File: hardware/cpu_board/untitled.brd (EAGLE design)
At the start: 126.3 x 94.6 mm, 70 parts, among them IC1 MAX232ECWE, IC2 MAX232ECWE, IC3 AM29F040J, IC4 74HCT138D, IC5 LM2596S, J2 POWER_JACKSLT, U1 AS6C4008-55SIN

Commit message: PCB update
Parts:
- moved C2 64.8 mm to (-11.3, 7.32)
- moved C3 59.9 mm to (16.7, -7.29)
- moved R15 59.9 mm to (15.3, -7.29)
- moved U$4 59.5 mm to (42.2, 36.9)
- moved C15 45.3 mm to (4.06, -8.51)
- moved U$3 45.3 mm to (7.09, -6.92)
- moved C1 42.5 mm to (27.0, -10.8)
- moved R4 31.5 mm to (41.2, -7.21)
- moved R6 30.2 mm to (40.2, -3.91)
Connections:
- net !BUSACK: now also U$4.78
- net !BUSREQ: now also U$4.79
- net !INT: now also U$4.4
- net !IRQ1: now also U$4.5
- net !IRQ2: now also U$4.6
- net !NMI: now also U$4.1
- net !RD: now also U$4.70
- net !RST: now also U$4.80
- net !WAIT: now also U$4.77
- net !WR: now also U$4.69
- net 5V: now also U$4.32
- net A0: now also U$4.8
- net A1: now also U$4.9
- net A10: now also U$4.20
- net A11: now also U$4.21
- net A12: now also U$4.24
- net A13: now also U$4.25
- net A14: now also U$4.26
- net A15: now also U$4.27
- net A16: now also U$4.28
- net A17: now also U$4.29
- net A18: now also U$4.31
- net A2: now also U$4.10
- net A3: now also U$4.11
- net A4: now also U$4.13
- net A5: now also U$4.15
- net A6: now also U$4.16
- net A7: now also U$4.17
- net A8: now also U$4.18
- net A9: now also U$4.19
- net CLK: now also U$4.71
- net CTS1: now also U$4.46
- net CTS2: now also U$4.57
- net D0: now also U$4.35
- net D1: now also U$4.36
- net D2: now also U$4.37
- net D3: now also U$4.38
- net D4: now also U$4.39
- net D5: now also U$4.40
- net D6: now also U$4.41
- net D7: now also U$4.44
- net GND: now also U$4.12, U$4.34, U$4.72, U$4.73
- net RTS1: now also U$4.45
- net RXD1: now also U$4.49
- net RXD2: now also U$4.54
- net ST: now also U$4.7
- net TXD1: now also U$4.48
- net TXD2: now also U$4.52
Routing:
- net 5V: track 497.4 -> 451.8 mm
- net !IORQ: track 171.8 -> 137.6 mm
- net !M1: track 167.2 -> 133.3 mm
- net D1: track 159.3 -> 126.5 mm, vias 4 -> 2
- net !WR: track 196.8 -> 165.5 mm
- net !RD: track 205.6 -> 175.4 mm
- net CLK: track 101.2 -> 72.1 mm
- net D2: track 153.2 -> 129.1 mm, vias 4 -> 2
- net RTS1: track 52.6 -> 29.0 mm
- net CTS1: track 51.3 -> 28.0 mm
- net D3: track 131.3 -> 110.0 mm, vias 3 -> 1
- net !ROM_CS: track 47.4 -> 26.9 mm, vias 2 -> 1
- net RTS2: track 32.8 -> 12.2 mm
- net D5: track 124.8 -> 104.5 mm, vias 3 -> 1
- net D0: track 146.4 -> 126.2 mm, vias 3 -> 2
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
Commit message: PCB updated
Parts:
- removed U$3: ASE, crystal:ASE
- added C16, C32: (no value), rcl:C0603
- added Y1: CRYSTAL-GROUNDEDSMD-5X3.2, SparkFun-Clocks:CRYSTAL-SMD-5X3.2-4PAD
- R4, R6: device rcl:R0603 -> rcl:R0402
- moved C1 56.9 mm to (57.1, 37.4), turned to 90 degrees
- moved R4 32.9 mm to (35.2, 25.2)
- moved R6 24.1 mm to (32.0, 18.7)
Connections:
- removed net OSC_IN: U$3.3
- new net EXTAL: C16.1, U$4.76, Y1.3
- new net XTAL: C32.1, U$4.74, Y1.1
- net 5V: no longer U$3.4
- net GND: now also C16.2, C32.2, Y1.2, Y1.4; no longer U$3.2
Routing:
- net !WR: track 165.5 -> 197.6 mm
- net !RD: track 175.4 -> 206.7 mm
- net CLK: track 72.1 -> 102.5 mm
- net D0: track 126.2 -> 142.7 mm
- net D1: track 126.5 -> 142.1 mm
- net D2: track 129.1 -> 144.4 mm
- net D3: track 110.0 -> 125.0 mm
- net XTAL: track 0.00 -> 8.82 mm
- net EXTAL: track 0.00 -> 6.46 mm
- net !INT: track 74.7 -> 78.8 mm
- net 5V: track 451.8 -> 455.6 mm, vias 11 -> 12
- net !IRQ2: track 108.4 -> 109.9 mm
- net !IRQ1: track 103.8 -> 104.9 mm

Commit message: PCB updated
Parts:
- removed C16, C32: (no value), rcl:C0603
- removed Y1: CRYSTAL-GROUNDEDSMD-5X3.2, SparkFun-Clocks:CRYSTAL-SMD-5X3.2-4PAD
- added R11: (no value), rcl:R0603
- added U$3: ASE, crystal:ASE
- R15: device rcl:R0402 -> rcl:R0603
- moved R15 54.1 mm to (30.2, 44.7), turned to 180 degrees
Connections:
- new net N$26: IC4.6, R11.1
- net !IORQ: now also U$4.65
- net !M1: no longer IC4.6
- net 5V: now also R11.2, U$3.4
- net EXTAL: now also U$3.3; no longer C16.1, Y1.3
- net GND: now also U$3.2; no longer C16.2, C32.2, Y1.2, Y1.4
- net N$25: now also U$4.59
- net XTAL: no longer C32.1, Y1.1
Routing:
- net !M1: track 133.3 -> 0.00 mm, vias 1 -> 0
- net !IORQ: track 137.6 -> 169.7 mm
- net TXD2: track 10.3 -> 38.6 mm
- net RTS1: track 29.0 -> 56.1 mm
- net RXD2: track 8.88 -> 35.5 mm
- net CTS1: track 28.0 -> 53.9 mm
- net TXD1: track 24.8 -> 49.1 mm
- net CTS2: track 13.2 -> 35.3 mm
- net RXD1: track 26.4 -> 44.7 mm
- net N$26: track 0.00 -> 12.2 mm, vias 0 -> 1
- net XTAL: track 8.82 -> 0.00 mm
- net N$25: track 0.00 -> 8.32 mm
- net RTS2: track 12.2 -> 4.62 mm
- net EXTAL: track 6.46 -> 3.40 mm
- net 5V: track 455.6 -> 458.6 mm, vias 12 -> 13
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
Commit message: Minor update
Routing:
- net RTS2: track 4.62 -> 10.8 mm
- net CTS2: track 35.3 -> 33.6 mm
- net TXD2: track 38.6 -> 40.0 mm
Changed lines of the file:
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@@
 <contactref element="C12" pad="2"/>
 <contactref element="C11" pad="2"/>
-<via x="17.145" y="42.545" extent="1-16" drill="0.6" diameter="1.4224" shape="octagon"/>
+<via x="17.145" y="45.72" extent="1-16" drill="0.6" diameter="1.4224" shape="octagon"/>
 <via x="24.0792" y="67.31" extent="1-16" drill="0.6" diameter="1.4224" shape="octagon"/>
 <via x="15.875" y="48.895" extent="1-16" drill="0.6" diameter="1.4224" shape="octagon"/>
@@
 <signal name="TXD2">
 <contactref element="IC1" pad="11"/>
-<wire x1="17.78" y1="30.9372" x2="17.78" y2="34.29" width="0.4064" layer="16"/>
-<via x="17.78" y="34.29" extent="1-16" drill="0.6" diameter="1.4224" shape="octagon"/>
+<wire x1="17.78" y1="30.9372" x2="17.78" y2="40.5892" width="0.4064" layer="16"/>
+<via x="17.78" y="40.5892" extent="1-16" drill="0.6" diameter="1.4224" shape="octagon"/>
 <contactref element="U$4" pad="52"/>
-<wire x1="17.78" y1="34.29" x2="17.78" y2="35.9664" width="0.3048" layer="1"/>
-<wire x1="17.78" y1="35.9664" x2="25.4" y2="43.5864" width="0.3048" layer="1"/>
-<wire x1="25.4" y1="43.5864" x2="25.4" y2="45.8216" width="0.3048" layer="1"/>
-<wire x1="25.4" y1="45.8216" x2="27.7368" y2="48.1584" width="0.3048" layer="1"/>
-<wire x1="27.7368" y1="48.1584" x2="41.6052" y2="48.1584" width="0.3048" layer="1"/>
+<wire x1="26.9494" y1="48.1584" x2="41.6052" y2="48.1584" width="0.3048" layer="1"/>
 <wire x1="41.6052" y1="48.1584" x2="43.0402" y2="46.7234" width="0.3048" layer="1"/>
 <wire x1="43.0402" y1="45.3254" x2="43.0402" y2="46.7234" width="0.3048" layer="1"/>
+<wire x1="17.78" y1="40.5892" x2="19.3802" y2="40.5892" width="0.3048" layer="1"/>
+<wire x1="26.9494" y1="48.1584" x2="19.3802" y2="40.5892" width="0.3048" layer="1"/>
 </signal>
 <signal name="RTS2">
 <contactref element="IC1" pad="10"/>
-<wire x1="16.51" y1="30.9372" x2="16.51" y2="35.56" width="0.4064" layer="16"/>
-<via x="16.51" y="35.56" extent="1-16" drill="0.6" diameter="1.4224" shape="octagon"/>
+<wire x1="16.51" y1="30.9372" x2="16.51" y2="41.783" width="0.4064" layer="16"/>
+<via x="16.51" y="41.783" extent="1-16" drill="0.6" diameter="1.4224" shape="octagon"/>
 </signal>
 <signal name="RXD2">
 <contactref element="IC1" pad="12"/>
-<wire x1="19.05" y1="30.9372" x2="19.05" y2="35.56" width="0.4064" layer="16"/>
-<via x="19.05" y="35.56" extent="1-16" drill="0.6" diameter="1.4224" shape="octagon"/>
+<wire x1="19.05" y1="30.9372" x2="19.05" y2="39.3954" width="0.4064" layer="16"/>
+<via x="19.05" y="39.3954" extent="1-16" drill="0.6" diameter="1.4224" shape="octagon"/>
 <contactref element="U$4" pad="54"/>
-<wire x1="19.05" y1="36.0172" x2="26.0096" y2="42.9768" width="0.3048" layer="1"/>
-<wire x1="26.0096" y1="42.9768" x2="26.0096" y2="45.5676" width="0.3048" layer="1"/>
-<wire x1="26.0096" y1="45.5676" x2="27.9908" y2="47.5488" width="0.3048" layer="1"/>
-<wire x1="27.9908" y1="47.5488" x2="40.6146" y2="47.5488" width="0.3048" layer="1"/>
+<wire x1="27.2034" y1="47.5488" x2="40.6146" y2="47.5488" width="0.3048" layer="1"/>
 <wire x1="40.6146" y1="47.5488" x2="41.4402" y2="46.7232" width="0.3048" layer="1"/>
 <wire x1="41.4402" y1="45.3254" x2="41.4402" y2="46.7232" width="0.3048" layer="1"/>
-<wire x1="19.05" y1="35.56" x2="19.05" y2="36.0172" width="0.3048" layer="1"/>
+<wire x1="27.2034" y1="47.5488" x2="19.05" y2="39.3954" width="0.3048" layer="1"/>
 </signal>
 <signal name="CTS2">
 <contactref element="IC1" pad="9"/>
-<wire x1="15.24" y1="30.9372" x2="15.24" y2="33.02" width="0.4064" layer="16"/>
-<via x="15.24" y="33.02" extent="1-16" drill="0.6" diameter="1.4224" shape="octagon"/>
+<wire x1="15.24" y1="30.9372" x2="15.24" y2="33.9344" width="0.4064" layer="16"/>
+<via x="15.24" y="33.9344" extent="1-16" drill="0.6" diameter="1.4224" shape="octagon"/>
 <contactref element="U$4" pad="57"/>
-<wire x1="15.24" y1="33.02" x2="18.161" y2="33.02" width="0.3048" layer="1"/>
-<wire x1="20.2184" y1="36.322" x2="26.6192" y2="42.7228" width="0.3048" layer="1"/>
-<wire x1="26.6192" y1="42.7228" x2="26.6192" y2="45.3136" width="0.3048" layer="1"/>
-<wire x1="26.6192" y1="45.3136" x2="28.2448" y2="46.9392" width="0.3048" layer="1"/>
 <wire x1="28.2448" y1="46.9392" x2="38.6842" y2="46.9392" width="0.3048" layer="1"/>
 <wire x1="38.6842" y1="46.9392" x2="39.0402" y2="46.5832" width="0.3048" layer="1"/>
 <wire x1="39.0402" y1="45.3254" x2="39.0402" y2="46.5832" width="0.3048" layer="1"/>
-<wire x1="18.161" y1="33.02" x2="20.2184" y2="35.0774" width="0.3048" layer="1"/>
-<wire x1="20.2184" y1="35.0774" x2="20.2184" y2="36.322" width="0.3048" layer="1"/>
+<wire x1="15.24" y1="33.9344" x2="28.2448" y2="46.9392" width="0.3048" layer="1"/>
 </signal>
 <signal name="N$20">

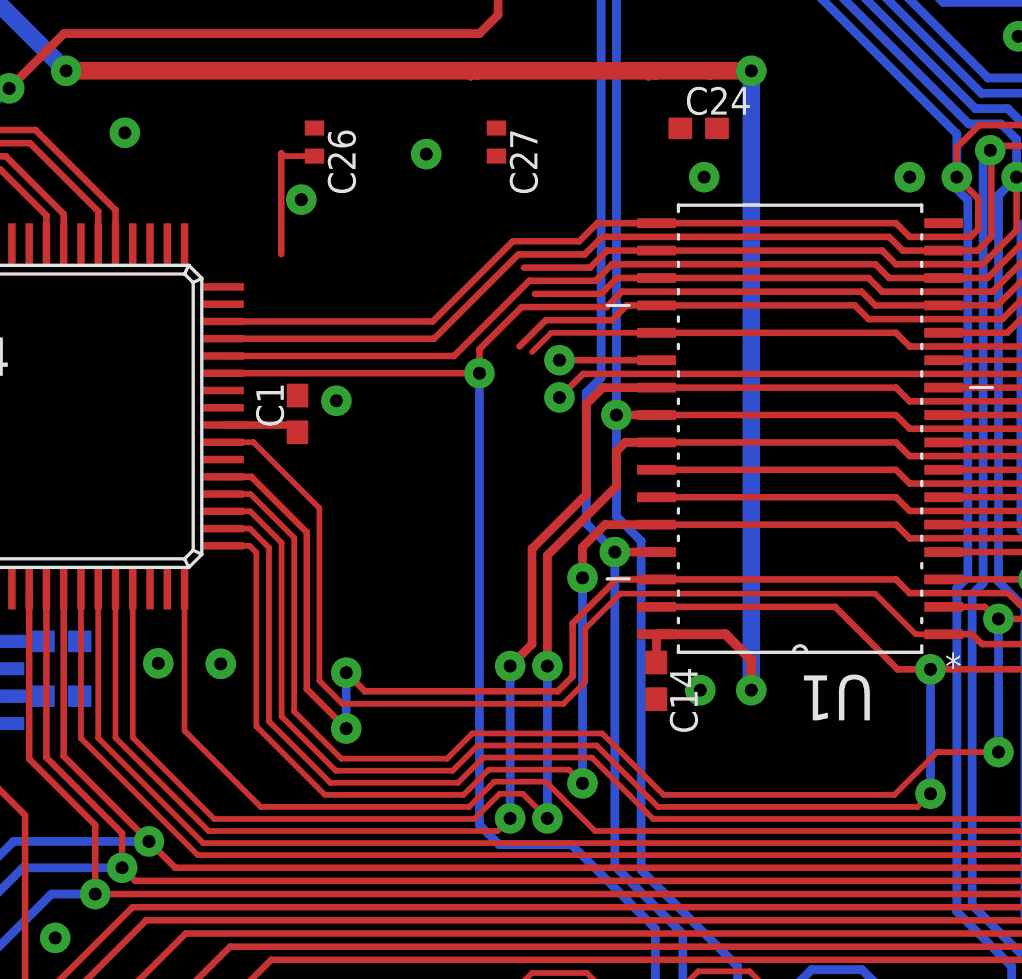
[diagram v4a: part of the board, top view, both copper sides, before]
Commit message: Data lines routed
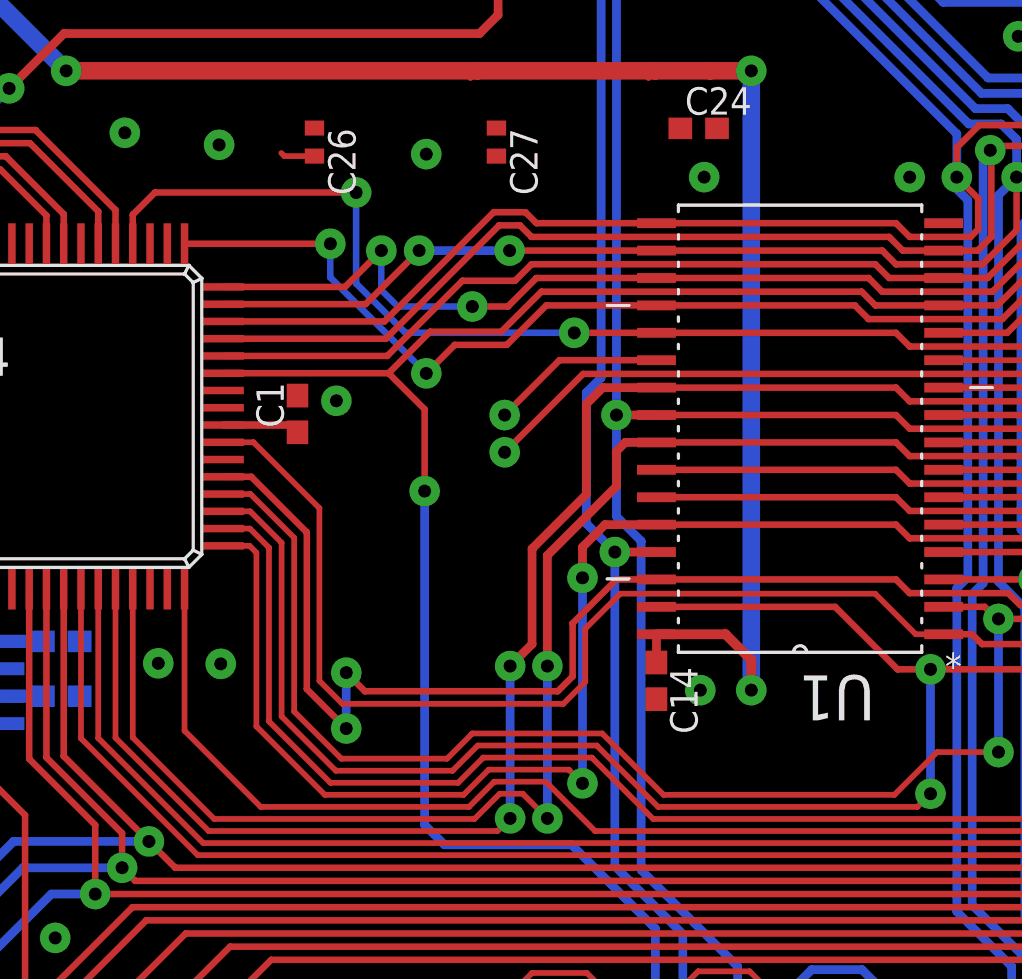
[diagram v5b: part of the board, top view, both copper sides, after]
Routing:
- net D7: track 77.6 -> 102.7 mm, vias 1 -> 3
- net D6: track 105.5 -> 125.2 mm, vias 1 -> 3
- net D5: track 104.5 -> 122.0 mm, vias 1 -> 3
- net D4: track 106.7 -> 121.3 mm, vias 1 -> 3
- net GND: track 71.1 -> 66.4 mm
- net !ROM_CS: track 26.9 -> 30.5 mm
- net !RAM_CS: track 4.50 -> 8.09 mm
- net D0: track 142.7 -> 145.3 mm

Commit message: Another update
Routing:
- net !RST: track 165.2 -> 168.0 mm, vias 4 -> 2
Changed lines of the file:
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@@
 <wire x1="83.8581" y1="42.4688" x2="83.2231" y2="43.1038" width="0.3048" layer="1"/>
 <wire x1="83.2231" y1="43.1038" x2="68.3768" y2="43.1038" width="0.3048" layer="1"/>
-<via x="62.9666" y="33.8644" extent="1-16" drill="0.6" diameter="1.4224" shape="octagon"/>
+<via x="62.9666" y="26.8794" extent="1-16" drill="0.6" diameter="1.4224" shape="octagon"/>
 <wire x1="98.1456" y1="46.609" x2="97.3328" y2="47.4218" width="0.3048" layer="1"/>
-<wire x1="62.9666" y1="33.8644" x2="62.9666" y2="18.3896" width="0.4064" layer="16"/>
+<wire x1="62.9666" y1="26.8794" x2="62.9666" y2="18.3896" width="0.4064" layer="16"/>
 <wire x1="62.9666" y1="18.3896" x2="63.881" y2="17.4752" width="0.4064" layer="16"/>
 <wire x1="63.881" y1="17.4752" x2="69.7738" y2="17.4752" width="0.4064" layer="16"/>
@@
 <wire x1="66.5226" y1="41.2496" x2="68.3768" y2="43.1038" width="0.3048" layer="1"/>
 <wire x1="63.2206" y1="41.2496" x2="61.2964" y2="39.3254" width="0.3048" layer="1"/>
-<wire x1="62.9666" y1="33.8644" x2="62.9666" y2="37.6552" width="0.3048" layer="1"/>
+<wire x1="62.9666" y1="26.8794" x2="62.9666" y2="37.6552" width="0.3048" layer="1"/>
 <wire x1="62.9666" y1="37.6552" x2="61.2964" y2="39.3254" width="0.3048" layer="1"/>
 </signal>
@@
 <wire x1="59.7916" y1="43.4848" x2="62.0776" y2="41.1988" width="0.3048" layer="16"/>
 <wire x1="50.4698" y1="47.7012" x2="59.7916" y2="47.7012" width="0.3048" layer="1"/>
-<via x="69.9008" y="41.1988" extent="1-16" drill="0.6" diameter="1.4224" shape="octagon"/>
-<wire x1="73.7108" y1="41.1988" x2="69.9008" y2="41.1988" width="0.3048" layer="1"/>
-<wire x1="69.9008" y1="41.1988" x2="62.0776" y2="41.1988" width="0.3048" layer="16"/>
+<via x="69.0372" y="41.2242" extent="1-16" drill="0.6" diameter="1.4224" shape="octagon"/>
+<wire x1="73.7108" y1="41.1988" x2="69.0372" y2="41.2242" width="0.3048" layer="1"/>
+<wire x1="69.0372" y1="41.2242" x2="62.0776" y2="41.1988" width="0.3048" layer="16"/>
 </signal>
 <signal name="!IORQ">
@@
 <wire x1="38.1162" y1="23.0886" x2="39.5732" y2="23.0886" width="0.4064" layer="16"/>
 <wire x1="39.5732" y1="23.0886" x2="39.9034" y2="23.4188" width="0.4064" layer="16"/>
-<wire x1="70.4342" y1="60.1218" x2="70.4342" y2="67.9958" width="0.4064" layer="16"/>
 <wire x1="70.4342" y1="67.9958" x2="73.7108" y2="71.2724" width="0.4064" layer="16"/>
 <wire x1="73.7108" y1="71.2724" x2="93.8276" y2="71.2724" width="0.4064" layer="16"/>
 <wire x1="93.8276" y1="71.2724" x2="94.9325" y2="70.1675" width="0.4064" layer="16"/>
 <wire x1="94.9325" y1="66.31" x2="94.9325" y2="70.1675" width="0.4064" layer="16"/>
-<wire x1="69.5706" y1="59.2582" x2="70.4342" y2="60.1218" width="0.4064" layer="16"/>
-<via x="43.7134" y="52.5272" extent="1-16" drill="0.6" diameter="1.4224" shape="octagon"/>
-<wire x1="65.5066" y1="55.0672" x2="66.3702" y2="55.9308" width="0.4064" layer="1"/>
-<wire x1="66.3702" y1="55.9308" x2="66.3702" y2="59.2582" width="0.4064" layer="1"/>
-<via x="66.3702" y="59.2582" extent="1-16" drill="0.6" diameter="1.4224" shape="octagon"/>
-<wire x1="66.3702" y1="59.2582" x2="69.5706" y2="59.2582" width="0.4064" layer="16"/>
-<wire x1="65.5066" y1="55.0672" x2="46.2534" y2="55.0672" width="0.4064" layer="1"/>
-<wire x1="46.2534" y1="55.0672" x2="43.7134" y2="52.5272" width="0.4064" layer="1"/>
-<wire x1="39.9034" y1="23.4188" x2="39.9034" y2="29.845" width="0.4064" layer="16"/>
-<wire x1="39.9034" y1="29.845" x2="39.9034" y2="48.7172" width="0.4064" layer="16"/>
-<wire x1="39.9034" y1="48.7172" x2="43.7134" y2="52.5272" width="0.4064" layer="16"/>
+<wire x1="39.9034" y1="23.4188" x2="39.9034" y2="29.972" width="0.4064" layer="16"/>
 <wire x1="38.1162" y1="23.0886" x2="36.83" y2="23.0886" width="0.6096" layer="16"/>
 <wire x1="36.83" y1="23.0886" x2="35.1913" y2="23.0886" width="0.6096" layer="16"/>
@@
 <wire x1="31.6402" y1="31.3254" x2="31.5976" y2="31.3254" width="0.3048" layer="1"/>
 <wire x1="31.5976" y1="31.3254" x2="31.5976" y2="29.972" width="0.3048" layer="1"/>
-<wire x1="31.5976" y1="29.972" x2="39.8018" y2="29.972" width="0.4064" layer="16"/>
-<wire x1="39.8018" y1="29.972" x2="39.9034" y2="29.845" width="0.4064" layer="16"/>
+<wire x1="31.5976" y1="29.972" x2="39.9034" y2="29.972" width="0.4064" layer="16"/>
+<wire x1="70.4342" y1="67.9958" x2="70.4342" y2="39.4208" width="0.4064" layer="16"/>
+<wire x1="70.4342" y1="39.4208" x2="69.7484" y2="38.735" width="0.4064" layer="16"/>
+<wire x1="69.7484" y1="38.735" x2="69.7484" y2="32.512" width="0.4064" layer="16"/>
+<wire x1="39.9034" y1="29.972" x2="67.2084" y2="29.972" width="0.4064" layer="16"/>
+<wire x1="67.2084" y1="29.972" x2="69.7484" y2="32.512" width="0.4064" layer="16"/>
 </signal>
 <signal name="!M1">

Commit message: PCB update
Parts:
- moved C24 75.9 mm to (32.3, -11.5), turned to 270 degrees
- moved C27 71.4 mm to (30.1, -11.6)
- moved C26 68.4 mm to (28.0, -11.6)
- moved C21 1.91 mm to (45.3, 64.1)
- moved C20 1.91 mm to (31.9, 79.4)
- moved C23 1.91 mm to (39.6, 64.8)
- moved C28 1.91 mm to (29.9, 69.4)
- moved D1 1.91 mm to (27.1, 72.4)
- moved IC5 1.91 mm to (33.0, 61.6)
- moved L2 1.91 mm to (52.8, 71.5)
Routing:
- net 5V: track 458.6 -> 479.8 mm, vias 13 -> 14
- net GND: track 66.4 -> 65.0 mm
- net N$22: track 27.4 -> 26.2 mm

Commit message: PCB update
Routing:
- net 5V: track 479.8 -> 476.4 mm
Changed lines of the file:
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@@
 <wire x1="59.69" y1="86.5452" x2="59.69" y2="86.5486" width="1.0668" layer="1"/>
 <contactref element="C22" pad="+"/>
-<wire x1="59.69" y1="86.5486" x2="59.69" y2="88.9" width="1.0668" layer="1"/>
-<wire x1="59.69" y1="88.9" x2="59.69" y2="89.6366" width="1.0668" layer="1"/>
+<wire x1="59.69" y1="86.5486" x2="59.69" y2="89.6366" width="1.0668" layer="1"/>
 <wire x1="27.7994" y1="56.9468" x2="27.7994" y2="50.165" width="0.8128" layer="16"/>
 <wire x1="27.7994" y1="50.165" x2="27.7994" y2="44.7412" width="0.8128" layer="16"/>
@@
 <wire x1="52.2732" y1="56.9468" x2="55.88" y2="53.34" width="0.8128" layer="16"/>
 <via x="91.1216" y="59.1194" extent="1-16" drill="0.6" diameter="1.4224" shape="octagon"/>
-<wire x1="109.22" y1="91.44" x2="119.0752" y2="81.5848" width="1.0668" layer="1"/>
+<wire x1="114.1114" y1="86.5486" x2="119.0752" y2="81.5848" width="1.0668" layer="1"/>
 <wire x1="119.0752" y1="56.388" x2="119.0752" y2="65.20024375" width="1.0668" layer="1"/>
 <wire x1="119.0752" y1="65.20024375" x2="119.0752" y2="81.5848" width="1.0668" layer="1"/>
@@
 <wire x1="102.66524375" y1="65.20024375" x2="100.0506" y2="62.5856" width="1.0668" layer="1"/>
 <wire x1="100.0506" y1="59.1194" x2="100.0506" y2="62.5856" width="1.0668" layer="1"/>
-<wire x1="59.69" y1="88.9" x2="68.58" y2="88.9" width="1.0668" layer="1"/>
-<wire x1="68.58" y1="88.9" x2="71.12" y2="91.44" width="1.0668" layer="1"/>
-<wire x1="71.12" y1="91.44" x2="102.235" y2="91.44" width="1.0668" layer="1"/>
-<wire x1="102.235" y1="91.44" x2="109.22" y2="91.44" width="1.0668" layer="1"/>
 <contactref element="C24" pad="1"/>
 <contactref element="C26" pad="1"/>
@@
 <contactref element="C15" pad="1"/>
 <wire x1="4.064" y1="-7.659" x2="4.064" y2="-6.0979" width="0.6096" layer="1"/>
-<wire x1="102.0064" y1="91.2114" x2="102.235" y2="91.44" width="0.6096" layer="1"/>
 <wire x1="76.1864" y1="53.3536" x2="76.2" y2="53.34" width="0.3048" layer="1"/>
 <contactref element="U$4" pad="32"/>
@@
 <wire x1="55.88" y1="53.34" x2="55.88" y2="39.3836" width="0.8128" layer="16"/>
 <wire x1="55.88" y1="39.3836" x2="58.674" y2="36.5896" width="0.8128" layer="16"/>
+<wire x1="59.69" y1="86.5486" x2="114.1114" y2="86.5486" width="1.0668" layer="1"/>
 <wire x1="32.258" y1="-10.6816" x2="31.75" y2="12.7" width="0" layer="19" extent="1-16"/>
 <wire x1="30.099" y1="-10.907" x2="32.258" y2="-10.6816" width="0" layer="19" extent="1-1"/>
